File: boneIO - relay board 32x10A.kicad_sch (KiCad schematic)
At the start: 115 parts, among them J1 Screw_Terminal_01x03, J10 Screw_Terminal_01x03, J11 Screw_Terminal_01x03, J12 Conn_02x04_Odd_Even, J13 Screw_Terminal_01x03, J14 Screw_Terminal_01x03, J15 Screw_Terminal_01x03, J16 Screw_Terminal_01x03, J17 Screw_Terminal_01x03, J2 Screw_Terminal_01x03, J3 Screw_Terminal_01x03, J4 Screw_Terminal_01x03, J5 Screw_Terminal_01x03, J6 Screw_Terminal_01x03, J7 Screw_Terminal_01x03, J8 Screw_Terminal_01x03, J9 Screw_Terminal_01x03, K1 HF32F/024-ZS3, K10 HF32F/024-ZS3, K11 HF32F/024-ZS3, K12 HF32F/024-ZS3, K13 HF32F/024-ZS3, K14 HF32F/024-ZS3, K15 HF32F/024-ZS3, K16 HF32F/024-ZS3, K17 HF32F/024-ZS3, K18 HF32F/024-ZS3, K19 HF32F/024-ZS3, K2 HF32F/024-ZS3, K20 HF32F/024-ZS3, K21 HF32F/024-ZS3, K22 HF32F/024-ZS3, K23 HF32F/024-ZS3, K24 HF32F/024-ZS3, K25 HF32F/024-ZS3, K26 HF32F/024-ZS3, K27 HF32F/024-ZS3, K28 HF32F/024-ZS3, K29 HF32F/024-ZS3, K3 HF32F/024-ZS3, K30 HF32F/024-ZS3, K31 HF32F/024-ZS3, K32 HF32F/024-ZS3, K4 HF32F/024-ZS3, K5 HF32F/024-ZS3, K6 HF32F/024-ZS3, K7 HF32F/024-ZS3, K8 HF32F/024-ZS3, K9 HF32F/024-ZS3, SW1 SW_DIP_x03, SW2 SW_DIP_x03, SW3 SW_DIP_x03, U1 PCF8575, U2 ULN2803A, U21 MCP9808_SO8, U22 LM75_MSOP, U3 ULN2803A, U4 PCF8575, U5 ULN2803A, U6 ULN2803A

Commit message: relay board 32x10A v0.1
Dodanie PCF8575
Dodanie MCP23017
Dodanie diody LL4148
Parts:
- added U3, U7: MCP23017_SS, Package_SO:SSOP-28_5.3x10.2mm_P0.65mm, symbol Interface_Expansion:MCP23017_SS
- renumbered C4 to C3, C3 to C4, R2 to R1, R1 to R2, U22 to U10, U3 to U4, U4 to U5, U5 to U6, U6 to U8, U21 to U9
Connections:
- net +3V3: now also U3.9 (VDD), U7.9 (VDD)
- net GND: now also U3.10 (VSS), U7.10 (VSS)
- net SCL: now also U3.12 (SCK), U7.12 (SCK)
- net SDA: now also U3.13 (SDA), U7.13 (SDA)
- net INT_02: now reaches C5.1, R5.2, U5.1 (INT)
- net INT_02: now also U7.18 (~{RESET})
- net P8_2: now reaches U5.13 (P10), U8.1 (I1)
- net P8_2: now also U7.21 (GPA0)
- net P9_2: now reaches U5.14 (P11), U8.2 (I2)
- net P9_2: now also U7.22 (GPA1)
- net P10_2: now reaches U5.15 (P12), U8.3 (I3)
- net P10_2: now also U7.23 (GPA2)
- net P11_2: now reaches U5.16 (P13), U8.4 (I4)
- net P11_2: now also U7.24 (GPA3)
- net P12_2: now reaches U5.17 (P14), U8.5 (I5)
- net P12_2: now also U7.25 (GPA4)
- net P13_2: now reaches U5.18 (P15), U8.6 (I6)
- net P13_2: now also U7.26 (GPA5)
- net P14_2: now reaches U5.19 (P16), U8.7 (I7)
- net P14_2: now also U7.27 (GPA6)
- net P15_2: now reaches U5.20 (P17), U8.8 (I8)
- net P15_2: now also U7.28 (GPA7)
- net A0_1: now reaches R4.1, SW1.4, U1.21 (A0)
- net A0_1: now also U3.15 (A0)
- net A1_1: now reaches R3.1, SW1.5, U1.2 (A1)
- net A1_1: now also U3.16 (A1)
- net A2_1: now reaches R2.1, SW1.6, U1.3 (A2)
- net A2_1: now also U3.17 (A2)
- net A2_2: now reaches R6.1, SW2.6, U5.3 (A2)
- net A2_2: now also U7.17 (A2)
- net A1_2: now reaches R7.1, SW2.5, U5.2 (A1)
- net A1_2: now also U7.16 (A1)
- net A0_2: now reaches R8.1, SW2.4, U5.21 (A0)
- net A0_2: now also U7.15 (A0)
- net P0_1: now reaches U1.4 (P00), U2.1 (I1)
- net P0_1: now also U3.1 (GPB0)
- net P1_1: now reaches U1.5 (P01), U2.2 (I2)
- net P1_1: now also U3.2 (GPB1)
- net P2_1: now reaches U1.6 (P02), U2.3 (I3)
- net P2_1: now also U3.3 (GPB2)
- net P3_1: now reaches U1.7 (P03), U2.4 (I4)
- net P3_1: now also U3.4 (GPB3)
- net P4_1: now reaches U1.8 (P04), U2.5 (I5)
- net P4_1: now also U3.5 (GPB4)
- net P5_1: now reaches U1.9 (P05), U2.6 (I6)
- net P5_1: now also U3.6 (GPB5)
- net P6_1: now reaches U1.10 (P06), U2.7 (I7)
- net P6_1: now also U3.7 (GPB6)
- net P7_1: now reaches U1.11 (P07), U2.8 (I8)
- net P7_1: now also U3.8 (GPB7)
- net P8_1: now reaches U1.13 (P10), U4.1 (I1)
- net P8_1: now also U3.21 (GPA0)
- net P9_1: now reaches U1.14 (P11), U4.2 (I2)
- net P9_1: now also U3.22 (GPA1)
- net P10_1: now reaches U1.15 (P12), U4.3 (I3)
- net P10_1: now also U3.23 (GPA2)
- net P11_1: now reaches U1.16 (P13), U4.4 (I4)
- net P11_1: now also U3.24 (GPA3)
- net P12_1: now reaches U1.17 (P14), U4.5 (I5)
- net P12_1: now also U3.25 (GPA4)
- net P13_1: now reaches U1.18 (P15), U4.6 (I6)
- net P13_1: now also U3.26 (GPA5)
- net P14_1: now reaches U1.19 (P16), U4.7 (I7)
- net P14_1: now also U3.27 (GPA6)
- net P15_1: now reaches U1.20 (P17), U4.8 (I8)
- net P15_1: now also U3.28 (GPA7)
- net P0_2: now reaches U5.4 (P00), U6.1 (I1)
- net P0_2: now also U7.1 (GPB0)
- net P1_2: now reaches U5.5 (P01), U6.2 (I2)
- net P1_2: now also U7.2 (GPB1)
- net P2_2: now reaches U5.6 (P02), U6.3 (I3)
- net P2_2: now also U7.3 (GPB2)
- net P3_2: now reaches U5.7 (P03), U6.4 (I4)
- net P3_2: now also U7.4 (GPB3)
- net P4_2: now reaches U5.8 (P04), U6.5 (I5)
- net P4_2: now also U7.5 (GPB4)
- net P5_2: now reaches U5.9 (P05), U6.6 (I6)
- net P5_2: now also U7.6 (GPB5)
- net P6_2: now reaches U5.10 (P06), U6.7 (I7)
- net P6_2: now also U7.7 (GPB6)
- net P7_2: now reaches U5.11 (P07), U6.8 (I8)
- net P7_2: now also U7.8 (GPB7)
- net INT_01: now reaches C1.1, R1.2, U1.1 (INT)
- net INT_01: now also U3.18 (~{RESET})
- no-connect marks 32 -> 36
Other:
- note removed: "MCP 3 ADDRESS 0x22"
- note removed: "MCP 4 ADDRESS 0x23"
- moved on the sheet: C1, C2, C3, C4, C5, C6, C7, C8, R1, R2, R3, R4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

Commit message: relay board 32x10A v0.1 (rev2)
rozdzielenie GND
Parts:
- added R14: 0k, Resistor_SMD:R_0805_2012Metric, symbol Device:R
- renumbered R9 to R10, R10 to R11, R11 to R12, R12 to R13, R13 to R9
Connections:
- net GND: now also R14.1; no longer C3.1, C4.1, C7.1, C8.1, J12.2 (Pin_2), J12.4 (Pin_4), U2.9 (GND), U4.9 (GND), U6.9 (GND), U8.9 (GND)
- new net GND1: C3.1, C4.1, C7.1, C8.1, J12.2 (Pin_2), J12.4 (Pin_4), R14.2, U2.9 (GND), U4.9 (GND), U6.9 (GND), U8.9 (GND)

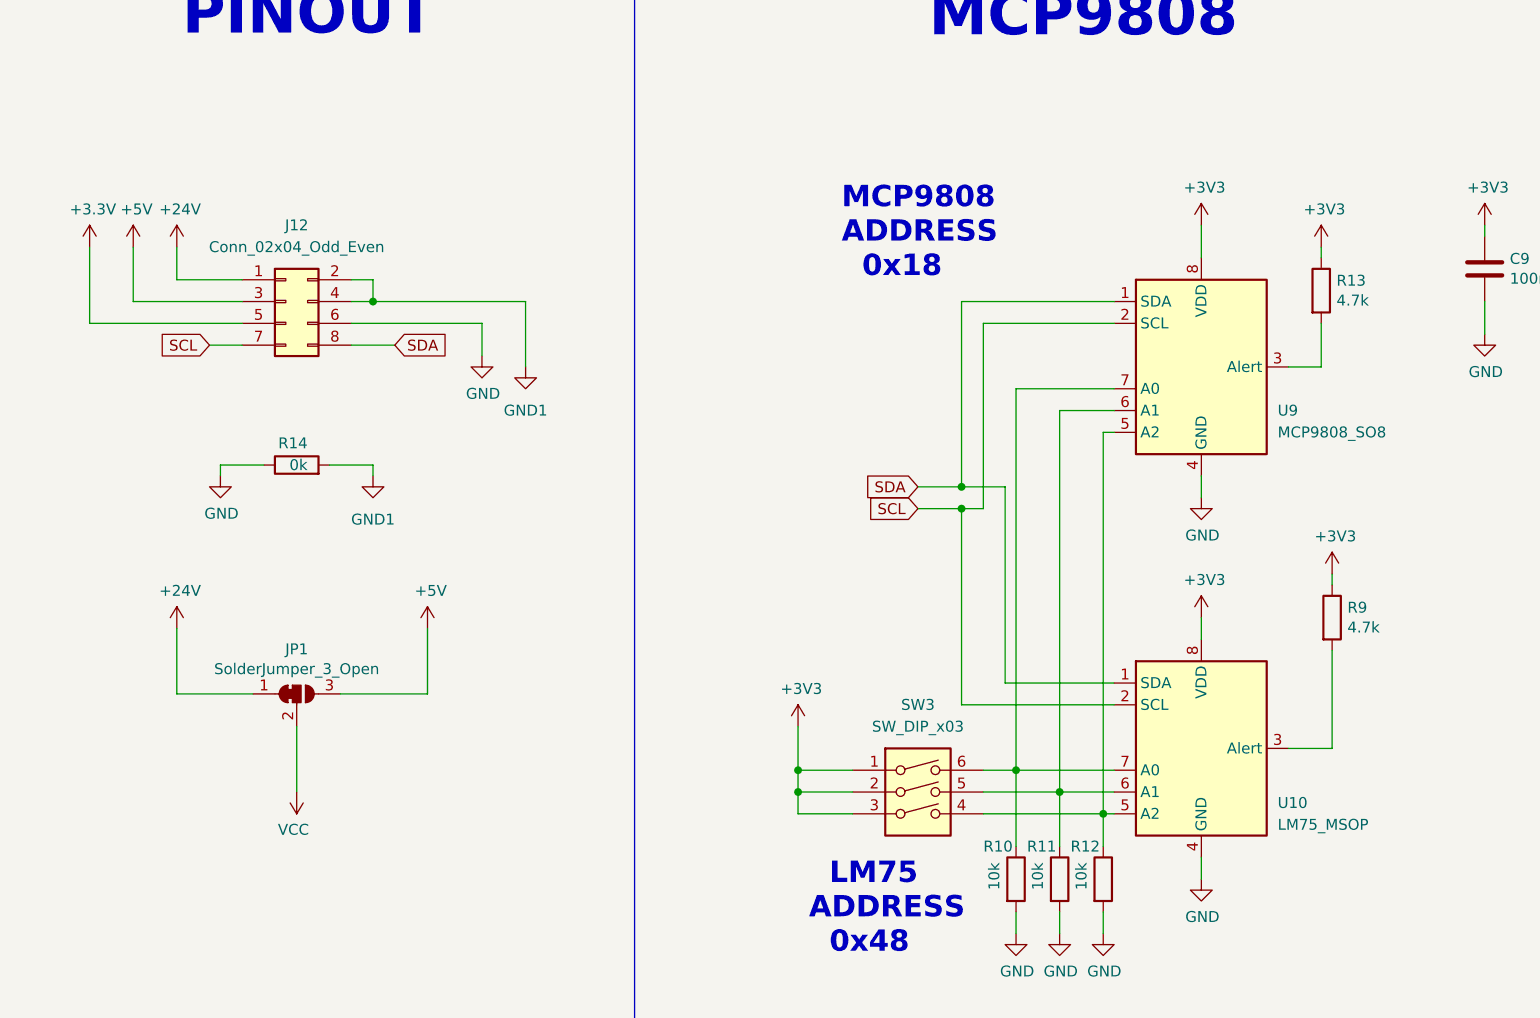
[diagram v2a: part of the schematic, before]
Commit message: v0.1
dodanie dławika filtrujacego
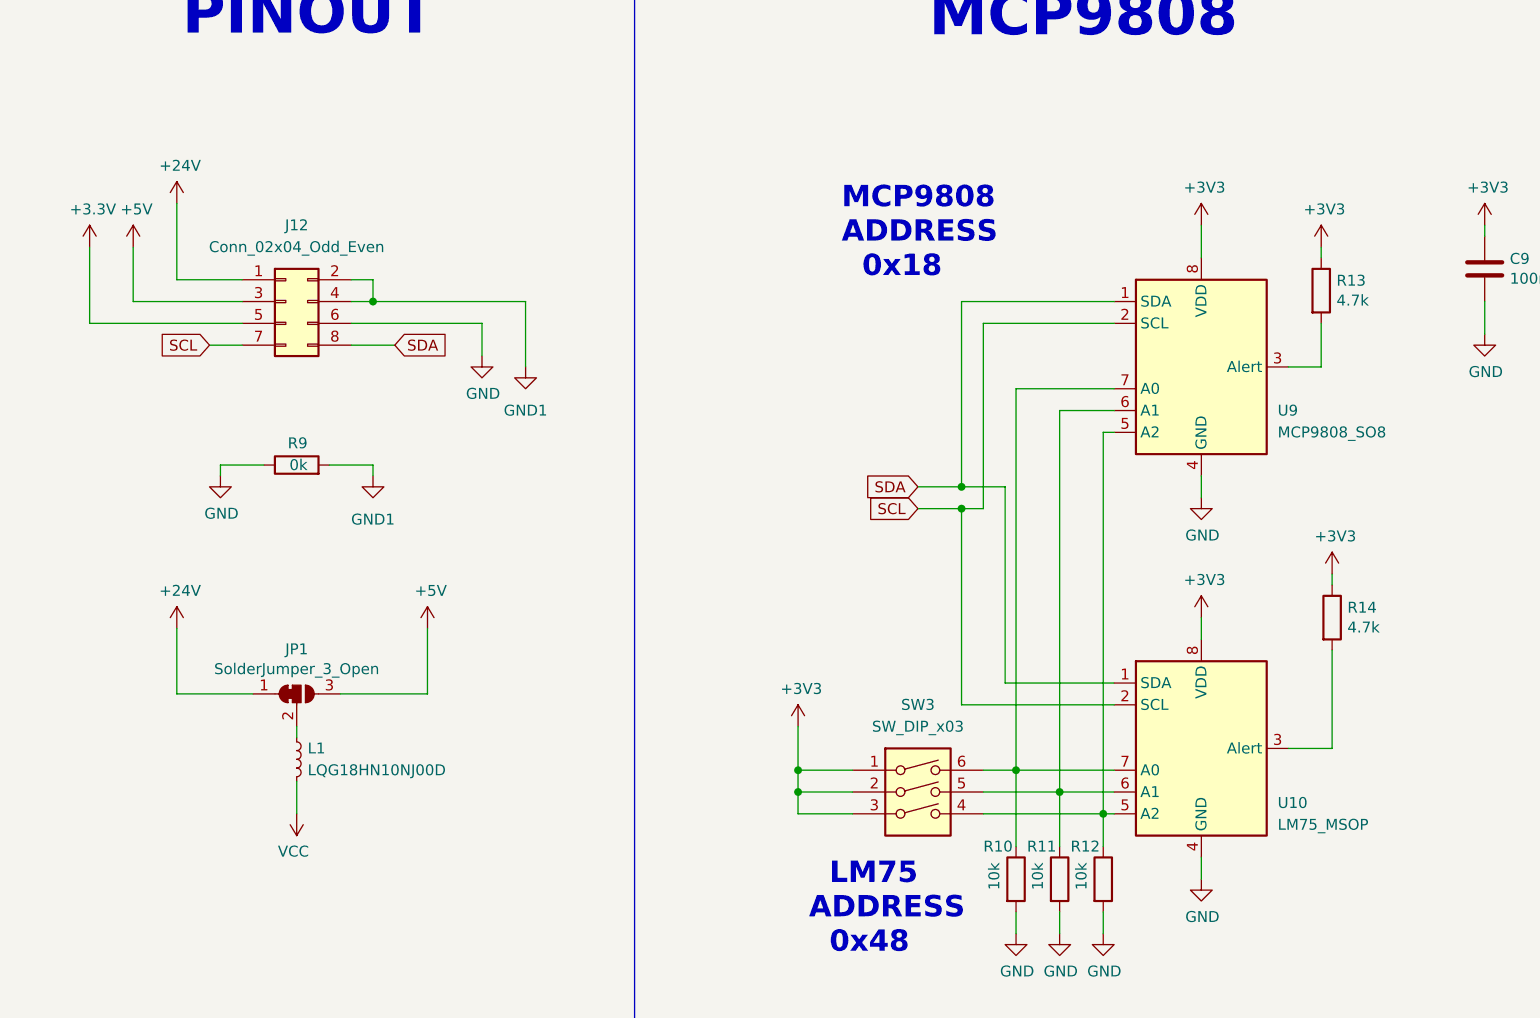
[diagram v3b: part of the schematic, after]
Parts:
- added L1: LQG18HN10NJ00D, Inductor_SMD:L_0603_1608Metric, symbol Device:L_Small
- renumbered R9 to R14, R14 to R9
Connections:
- net VCC: now also L1.2; no longer JP1.2 (C)
- new net: JP1.2 (C), L1.1
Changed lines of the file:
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@@
     (stroke (width 0) (type default) (color 0 0 0 0))
   )
+  (wire (pts (xy 422.91 127) (xy 422.91 130.81))
+    (stroke (width 0) (type default) (color 0 0 0 0))
+  )
   (wire (pts (xy 200.66 359.41) (xy 200.66 365.76))
     (stroke (width 0) (type default) (color 0 0 0 0))
@@
     (stroke (width 0) (type default) (color 0 0 0 0))
   )
-  (wire (pts (xy 408.94 68.58) (xy 408.94 64.77))
-    (stroke (width 0) (type default) (color 0 0 0 0))
-  )
   (wire (pts (xy 95.25 278.13) (xy 109.22 278.13))
     (stroke (width 0) (type default) (color 0 0 0 0))
@@
     (stroke (width 0) (type default) (color 0 0 0 0))
   )
-  (wire (pts (xy 422.91 120.65) (xy 422.91 128.27))
-    (stroke (width 0) (type default) (color 0 0 0 0))
-  )
   (wire (pts (xy 340.36 210.82) (xy 334.01 210.82))
     (stroke (width 0) (type default) (color 0 0 0 0))
@@
     (stroke (width 0) (type default) (color 0 0 0 0))
   )
+  (wire (pts (xy 408.94 59.69) (xy 408.94 68.58))
+    (stroke (width 0) (type default) (color 0 0 0 0))
+  )
   (wire (pts (xy 76.2 279.4) (xy 76.2 283.21))
     (stroke (width 0) (type default) (color 0 0 0 0))
@@
     (stroke (width 0) (type default) (color 0 0 0 0))
   )
+  (wire (pts (xy 422.91 120.65) (xy 422.91 121.92))
+    (stroke (width 0) (type default) (color 0 0 0 0))
+  )
   (wire (pts (xy 265.43 228.6) (xy 265.43 226.06))
     (stroke (width 0) (type default) (color 0 0 0 0))
@@
     (pin "1")
   )
-  (symbol (lib_id "power:VCC") (at 422.91 128.27 180) (unit 1)
+  (symbol (lib_id "power:VCC") (at 422.91 130.81 180) (unit 1)
     (in_bom yes) (on_board yes)
-    (property "Reference" "#PWR067" (id 0) (at 422.91 124.46 0)
+    (property "Reference" "#PWR067" (id 0) (at 422.91 127 0)
       (effects (font (size 1.27 1.27)) hide)
     )
-    (property "Value" "VCC" (id 1) (at 422.529 132.6642 0))
-    (property "Footprint" "" (id 2) (at 422.91 128.27 0)
+    (property "Value" "VCC" (id 1) (at 422.529 135.2042 0))
+    (property "Footprint" "" (id 2) (at 422.91 130.81 0)
       (effects (font (size 1.27 1.27)) hide)
     )
-    (property "Datasheet" "" (id 3) (at 422.91 128.27 0)
+    (property "Datasheet" "" (id 3) (at 422.91 130.81 0)
       (effects (font (size 1.27 1.27)) hide)
     )
@@
   (symbol (lib_id "Device:R") (at 543.56 107.95 0) (unit 1)
     (in_bom yes) (on_board yes)
-    (property "Reference" "R9" (id 0) (at 545.338 106.7816 0)
+    (property "Reference" "R14" (id 0) (at 545.338 106.7816 0)
       (effects (font (size 1.27 1.27)) (justify left))
     )
@@
     (pin "1")
   )
-  (symbol (lib_id "power:+24V") (at 408.94 64.77 0) (unit 1)
+  (symbol (lib_id "power:+24V") (at 408.94 59.69 0) (unit 1)
     (in_bom yes) (on_board yes)
-    (property "Reference" "#PWR064" (id 0) (at 408.94 68.58 0)
+    (property "Reference" "#PWR064" (id 0) (at 408.94 63.5 0)
       (effects (font (size 1.27 1.27)) hide)
     )
-    (property "Value" "+24V" (id 1) (at 409.321 60.3758 0))
-    (property "Footprint" "" (id 2) (at 408.94 64.77 0)
+    (property "Value" "+24V" (id 1) (at 409.321 55.2958 0))
+    (property "Footprint" "" (id 2) (at 408.94 59.69 0)
       (effects (font (size 1.27 1.27)) hide)
     )
-    (property "Datasheet" "" (id 3) (at 408.94 64.77 0)
+    (property "Datasheet" "" (id 3) (at 408.94 59.69 0)
       (effects (font (size 1.27 1.27)) hide)
     )
@@
     (pin "1")
   )
+  (symbol (lib_id "Device:L_Small") (at 422.91 124.46 0) (unit 1)
+    (in_bom yes) (on_board yes) (fields_autoplaced)
+    (property "Reference" "L1" (id 0) (at 424.18 123.1899 0)
+      (effects (font (size 1.27 1.27)) (justify left))
+    )
+    (property "Value" "LQG18HN10NJ00D" (id 1) (at 424.18 125.7299 0)
+      (effects (font (size 1.27 1.27)) (justify left))
+    )
+    (property "Footprint" "Inductor_SMD:L_0603_1608Metric" (id 2) (at 422.91 124.46 0)
+      (effects (font (size 1.27 1.27)) hide)
+    )
+    (property "Datasheet" "~" (id 3) (at 422.91 124.46 0)
+      (effects (font (size 1.27 1.27)) hide)
+    )
+    (pin "1")
+    (pin "2")
+  )
   (symbol (lib_id "Relay:HF32F{slash}024-ZS3") (at 105.41 285.75 180) (unit 1)
     (in_bom yes) (on_board yes)
@@
   (symbol (lib_id "Device:R") (at 422.91 90.17 90) (unit 1)
     (in_bom yes) (on_board yes)
-    (property "Reference" "R14" (id 0) (at 424.18 87.63 90)
+    (property "Reference" "R9" (id 0) (at 424.18 87.63 90)
       (effects (font (size 1.27 1.27)) (justify left))
     )
@@
       (reference "K32") (unit 1) (value "HF32F/024-ZS3") (footprint "relay-user:Realy_DPST_HF32F")
     )
+    (path "/2485c456-9935-4d6a-b317-13b9550fb79d"
+      (reference "L1") (unit 1) (value "LQG18HN10NJ00D") (footprint "Inductor_SMD:L_0603_1608Metric")
+    )
     (path "/b89082da-656c-454a-a04f-ae702e6ec249"
       (reference "R1") (unit 1) (value "4.7k") (footprint "Resistor_SMD:R_0603_1608Metric")
@@
       (reference "R8") (unit 1) (value "10k") (footprint "Resistor_SMD:R_0603_1608Metric")
     )
-    (path "/00000000-0000-0000-0000-000061aead31"
-      (reference "R9") (unit 1) (value "4.7k") (footprint "Resistor_SMD:R_0603_1608Metric")
+    (path "/34ca9643-55f1-41a0-8b8d-f013c74f3f19"
+      (reference "R9") (unit 1) (value "0k") (footprint "Resistor_SMD:R_0805_2012Metric")
     )
     (path "/00000000-0000-0000-0000-000061f1c0c6"
@@
       (reference "R13") (unit 1) (value "4.7k") (footprint "Resistor_SMD:R_0603_1608Metric")
     )
-    (path "/34ca9643-55f1-41a0-8b8d-f013c74f3f19"
-      (reference "R14") (unit 1) (value "0k") (footprint "Resistor_SMD:R_0805_2012Metric")
+    (path "/00000000-0000-0000-0000-000061aead31"
+      (reference "R14") (unit 1) (value "4.7k") (footprint "Resistor_SMD:R_0603_1608Metric")
     )
     (path "/83bb6872-55f3-432e-9f04-a0634e1d879a"

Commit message: relay board 32x10A
Final Version
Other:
- note added: "MCP23017 AND PCF8575"
- note added: "MCP23017, PCF8575 and ULN2803A"
- note added: "MCP9808 AND LM75"
- note removed: "MCP23017 and ULN2803A"
- note removed: "MCP9808"
- note removed: "PCF8575"
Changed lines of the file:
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@@
     (effects (font (size 5.0038 5.0038) (thickness 1.0008) bold) (justify left bottom))
   )
-  (text "MCP23017 and ULN2803A" (at 167.64 40.64 0)
+  (text "MCP23017, PCF8575 and ULN2803A" (at 127 41.91 0)
     (effects (font (size 5.0038 5.0038) (thickness 1.0008) bold) (justify left bottom))
   )
@@
     (effects (font (size 2.4892 2.4892) (thickness 0.4978) bold) (justify left bottom))
   )
-  (text "PCF8575" (at 252.73 334.01 0)
+  (text "MCP23017 AND PCF8575" (at 222.25 334.01 0)
     (effects (font (size 5.0038 5.0038) (thickness 1.0008) bold) (justify left bottom))
   )
@@
     (effects (font (size 5.0038 5.0038) (thickness 1.0008) bold) (justify left bottom))
   )
-  (text "MCP9808\n\n" (at 496.57 48.895 0)
+  (text "MCP9808 AND LM75\n\n" (at 480.06 49.53 0)
     (effects (font (size 5.0038 5.0038) (thickness 1.0008) bold) (justify left bottom))
   )
